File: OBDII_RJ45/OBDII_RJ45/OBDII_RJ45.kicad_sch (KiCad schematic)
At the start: 2 parts, among them J1 Cantact, J2 Conn_01x02

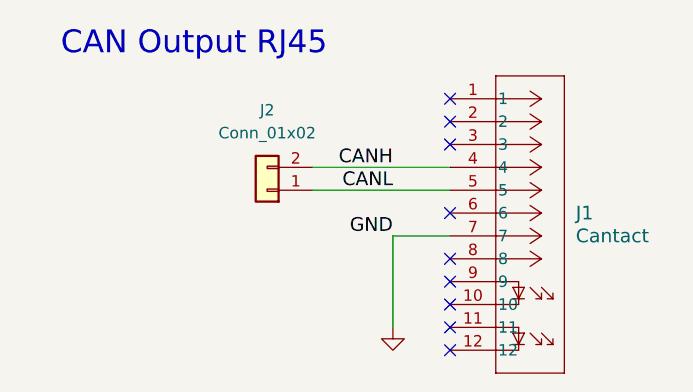
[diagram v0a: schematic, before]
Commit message: feat: add GND between OBDII connector & OBDII_RJ45
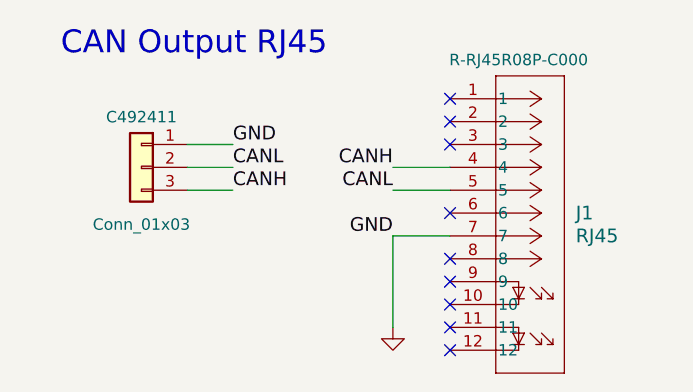
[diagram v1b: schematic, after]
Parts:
- removed J2: Conn_01x02, Connector_PinHeader_2.54mm:PinHeader_1x02_P2.54mm_Vertical, symbol Connector_Generic:Conn_01x02
- added J3: Conn_01x03, Connector_PinHeader_2.54mm:PinHeader_1x03_P2.54mm_Vertical, symbol Connector_Generic:Conn_01x03
- J1: value Cantact -> RJ45; #MANUF (none) -> R-RJ45R08P-C000
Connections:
- net CANH: now also J3.3 (Pin_3)
- net CANL: now also J3.2 (Pin_2)
- net GND: now also J3.1 (Pin_1)
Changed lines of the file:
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@@
 	(wire
 		(pts
-			(xy 43.18 31.75) (xy 58.42 31.75)
-		)
-		(stroke
-			(width 0)
-			(type default)
-		)
-	)
-	(wire
-		(pts
-			(xy 43.18 34.29) (xy 58.42 34.29)
+			(xy 52.07 34.29) (xy 58.42 34.29)
+		)
+		(stroke
+			(width 0)
+			(type default)
+		)
+	)
+	(wire
+		(pts
+			(xy 29.21 34.29) (xy 34.29 34.29)
+		)
+		(stroke
+			(width 0)
+			(type default)
+		)
+	)
+	(wire
+		(pts
+			(xy 52.07 31.75) (xy 58.42 31.75)
+		)
+		(stroke
+			(width 0)
+			(type default)
+		)
+	)
+	(wire
+		(pts
+			(xy 29.21 29.21) (xy 34.29 29.21)
+		)
+		(stroke
+			(width 0)
+			(type default)
+		)
+	)
+	(wire
+		(pts
+			(xy 29.21 31.75) (xy 34.29 31.75)
 		)
 		(stroke
@@
 		)
 	)
+	(label "GND"
+		(at 34.29 29.21 0)
+		(effects
+			(font
+				(size 1.524 1.524)
+			)
+			(justify left bottom)
+		)
+	)
 	(label "CANH"
 		(at 52.07 31.75 180)
@@
 			)
 			(justify right bottom)
+		)
+	)
+	(label "CANL"
+		(at 34.29 31.75 0)
+		(effects
+			(font
+				(size 1.524 1.524)
+			)
+			(justify left bottom)
+		)
+	)
+	(label "CANH"
+		(at 34.29 34.29 0)
+		(effects
+			(font
+				(size 1.524 1.524)
+			)
+			(justify left bottom)
 		)
 	)
@@
 			)
 		)
-		(property "Value" "Cantact"
+		(property "Value" "RJ45"
 			(at 72.39 39.3699 0)
 			(effects
@@
 			)
 		)
-		(property "Datasheet" "R-RJ45R08P-C000"
+		(property "Datasheet" "https://www.lcsc.com/datasheet/lcsc_datasheet_2411121108_Ckmtw-Shenzhen-Cankemeng-R-RJ45R08P-C000_C386757.pdf"
 			(at 56.896 18.796 0)
 			(effects
@@
 				)
 				(hide yes)
+			)
+		)
+		(property "#MANUF" "R-RJ45R08P-C000"
+			(at 66.04 19.812 0)
+			(effects
+				(font
+					(size 1.27 1.27)
+				)
 			)
 		)
@@
 	)
 	(symbol
-		(lib_id "Connector_Generic:Conn_01x02")
-		(at 38.1 34.29 180)
+		(lib_id "Connector_Generic:Conn_01x03")
+		(at 24.13 31.75 0)
+		(mirror y)
 		(unit 1)
 		(exclude_from_sim no)
@@
 		(on_board yes)
 		(dnp no)
-		(fields_autoplaced yes)
-		(property "Reference" "J2"
-			(at 38.1 25.4 0)
-			(effects
-				(font
-					(size 1.27 1.27)
-				)
-			)
-		)
-		(property "Value" "Conn_01x02"
-			(at 38.1 27.94 0)
-			(effects
-				(font
-					(size 1.27 1.27)
-				)
-			)
-		)
-		(property "Footprint" "Connector_PinHeader_2.54mm:PinHeader_1x02_P2.54mm_Vertical"
-			(at 38.1 34.29 0)
-			(effects
-				(font
-					(size 1.27 1.27)
-				)
-				(hide yes)
-			)
-		)
-		(property "Datasheet" "~"
-			(at 38.1 34.29 0)
-			(effects
-				(font
-					(size 1.27 1.27)
-				)
-				(hide yes)
-			)
-		)
-		(property "Description" "Generic connector, single row, 01x02, script generated (kicad-library-utils/schlib/autogen/connector/)"
-			(at 38.1 34.29 0)
-			(effects
-				(font
-					(size 1.27 1.27)
-				)
-				(hide yes)
-			)
-		)
-		(property "#MANUF" ""
-			(at 38.1 34.29 0)
+		(property "Reference" "J3"
+			(at 24.13 40.64 0)
+			(effects
+				(font
+					(size 1.27 1.27)
+				)
+				(hide yes)
+			)
+		)
+		(property "Value" "Conn_01x03"
+			(at 24.13 38.1 0)
+			(effects
+				(font
+					(size 1.27 1.27)
+				)
+			)
+		)
+		(property "Footprint" "Connector_PinHeader_2.54mm:PinHeader_1x03_P2.54mm_Vertical"
+			(at 24.13 31.75 0)
+			(effects
+				(font
+					(size 1.27 1.27)
+				)
+				(hide yes)
+			)
+		)
+		(property "Datasheet" "https://www.lcsc.com/datasheet/lcsc_datasheet_2409302300_XFCN-PZ254R-11-03P_C492411.pdf"
+			(at 24.13 31.75 0)
+			(effects
+				(font
+					(size 1.27 1.27)
+				)
+				(hide yes)
+			)
+		)
+		(property "Description" "Generic connector, single row, 01x03, script generated (kicad-library-utils/schlib/autogen/connector/)"
+			(at 24.13 31.75 0)
+			(effects
+				(font
+					(size 1.27 1.27)
+				)
+				(hide yes)
+			)
+		)
+		(property "#MANUF" "PZ254R-11-03P"
+			(at 24.13 31.75 0)
 			(effects
 				(font
@@
 		)
 		(property "PROVEEDOR" ""
-			(at 38.1 34.29 0)
-			(effects
-				(font
-					(size 1.27 1.27)
-				)
-				(hide yes)
+			(at 24.13 31.75 0)
+			(effects
+				(font
+					(size 1.27 1.27)
+				)
+				(hide yes)
+			)
+		)
+		(property "LCSC#" "C492411"
+			(at 24.13 26.162 0)
+			(effects
+				(font
+					(size 1.27 1.27)
+				)
 			)
 		)
@@
 		)
 		(pin "1"
+		)
+		(pin "3"
 		)
 		(instances
 			(project "OBDII_RJ45"
 				(path "/2550f002-d348-4526-bc52-f9a1d613dc79"
-					(reference "J2")
+					(reference "J3")
 					(unit 1)
 				)

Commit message: feat(Hw):Update_Labels
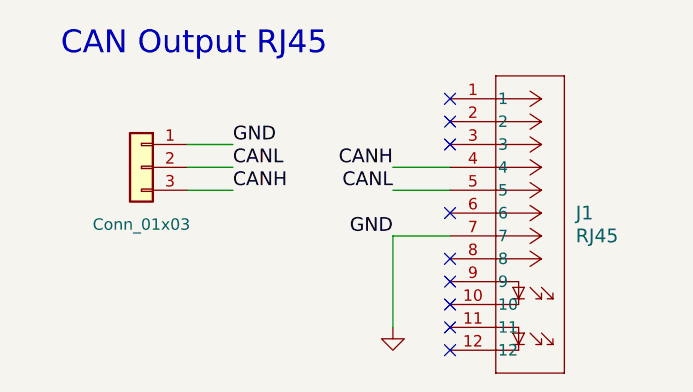
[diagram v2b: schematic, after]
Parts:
- J1: #MANUF R-RJ45R08P-C000 -> (none); manf# R-RJ45R08P-C000 -> (none)
- J3: #MANUF PZ254R-11-03P -> (none)
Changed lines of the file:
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@@
 			)
 		)
-		(property "manf#" "R-RJ45R08P-C000"
+		(property "manf#" ""
 			(at 68.834 20.32 0)
 			(effects
@@
 			)
 		)
-		(property "#MANUF" "R-RJ45R08P-C000"
+		(property "#MANUF" ""
 			(at 66.04 19.812 0)
 			(effects
@@
 			)
 		)
-		(property "#MANUF" "PZ254R-11-03P"
+		(property "#MANUF" ""
 			(at 24.13 31.75 0)
 			(effects
@@
 					(size 1.27 1.27)
 				)
+				(hide yes)
 			)
 		)

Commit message: Fix: CANbus routing for OBDII_RJ45
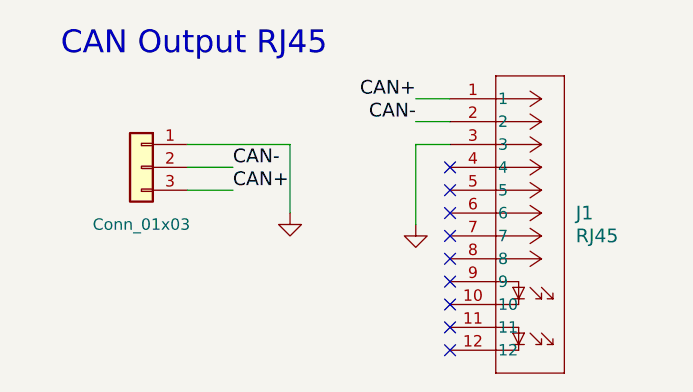
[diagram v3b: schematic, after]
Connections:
- net GND: now also J1.3; no longer J1.7
- net CAN+: now reaches J1.1
- net CAN+: now also J3.3 (Pin_3)
- net CAN-: now reaches J1.2
- net CAN-: now also J3.2 (Pin_2)
- net CANH: no longer names the net of J1.4
- net CANH: no longer J3.3 (Pin_3)
- net CANL: no longer names the net of J1.5
- net CANL: no longer J3.2 (Pin_2)
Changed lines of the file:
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@@
+	)
+	(no_connect
+		(at 58.42 31.75)
+	)
+	(no_connect
+		(at 58.42 34.29)
+	)
+	(no_connect
+		(at 58.42 39.37)
 	)
 	(no_connect
@@
 	)
 	(no_connect
-		(at 58.42 24.13)
-	)
-	(no_connect
 		(at 58.42 49.53)
 	)
@@
 	)
 	(no_connect
-		(at 58.42 26.67)
-	)
-	(no_connect
 		(at 58.42 52.07)
 	)
 	(no_connect
-		(at 58.42 29.21)
-	)
-	(no_connect
 		(at 58.42 44.45)
 	)
 	(wire
 		(pts
-			(xy 52.07 39.37) (xy 58.42 39.37)
-		)
-		(stroke
-			(width 0)
-			(type default)
-		)
-	)
-	(wire
-		(pts
-			(xy 52.07 39.37) (xy 52.07 49.53)
-		)
-		(stroke
-			(width 0)
-			(type default)
-		)
-	)
-	(wire
-		(pts
-			(xy 52.07 34.29) (xy 58.42 34.29)
+			(xy 54.61 38.1) (xy 54.61 29.21)
+		)
+		(stroke
+			(width 0)
+			(type default)
+		)
+	)
+	(wire
+		(pts
+			(xy 40.64 29.21) (xy 40.64 36.83)
+		)
+		(stroke
+			(width 0)
+			(type default)
+		)
+	)
+	(wire
+		(pts
+			(xy 54.61 24.13) (xy 58.42 24.13)
+		)
+		(stroke
+			(width 0)
+			(type default)
+		)
+	)
+	(wire
+		(pts
+			(xy 54.61 26.67) (xy 58.42 26.67)
 		)
 		(stroke
@@
 	(wire
 		(pts
-			(xy 52.07 31.75) (xy 58.42 31.75)
-		)
-		(stroke
-			(width 0)
-			(type default)
-		)
-	)
-	(wire
-		(pts
-			(xy 29.21 29.21) (xy 34.29 29.21)
+			(xy 54.61 29.21) (xy 58.42 29.21)
+		)
+		(stroke
+			(width 0)
+			(type default)
+		)
+	)
+	(wire
+		(pts
+			(xy 29.21 29.21) (xy 40.64 29.21)
 		)
 		(stroke
@@
 		)
 	)
-	(label "CANL"
-		(at 52.07 34.29 180)
+	(label "CAN+"
+		(at 34.29 34.29 0)
 		(effects
 			(font
 				(size 1.524 1.524)
 			)
-			(justify right bottom)
-		)
-	)
-	(label "GND"
-		(at 34.29 29.21 0)
+			(justify left bottom)
+		)
+	)
+	(label "CAN-"
+		(at 54.61 26.67 180)
 		(effects
 			(font
 				(size 1.524 1.524)
 			)
-			(justify left bottom)
-		)
-	)
-	(label "CANH"
-		(at 52.07 31.75 180)
-		(effects
-			(font
-				(size 1.524 1.524)
-			)
 			(justify right bottom)
 		)
 	)
-	(label "GND"
-		(at 52.07 39.37 180)
-		(effects
-			(font
-				(size 1.524 1.524)
-			)
-			(justify right bottom)
-		)
-	)
-	(label "CANL"
+	(label "CAN-"
 		(at 34.29 31.75 0)
 		(effects
@@
 		)
 	)
-	(label "CANH"
-		(at 34.29 34.29 0)
+	(label "CAN+"
+		(at 54.61 24.13 180)
 		(effects
 			(font
 				(size 1.524 1.524)
 			)
-			(justify left bottom)
+			(justify right bottom)
 		)
 	)
@@
 		(lib_name "GND_27")
 		(lib_id "cantact-rescue:GND")
-		(at 52.07 49.53 0)
+		(at 54.61 38.1 0)
 		(unit 1)
 		(exclude_from_sim no)
@@
 		(dnp no)
 		(property "Reference" "#PWR023"
-			(at 52.07 49.53 0)
+			(at 54.61 38.1 0)
 			(effects
 				(font
@@
 		)
 		(property "Value" "GND"
-			(at 52.07 51.308 0)
+			(at 54.61 39.878 0)
 			(effects
 				(font
@@
 		)
 		(property "Footprint" ""
-			(at 52.07 49.53 0)
+			(at 54.61 38.1 0)
 			(effects
 				(font
@@
 		)
 		(property "Datasheet" ""
-			(at 52.07 49.53 0)
+			(at 54.61 38.1 0)
 			(effects
 				(font
@@
 		)
 		(property "Description" ""
-			(at 52.07 49.53 0)
+			(at 54.61 38.1 0)
 			(effects
 				(font
@@
 					(unit 1)
 				)
+			)
+		)
+	)
+	(symbol
+		(lib_name "GND_27")
+		(lib_id "cantact-rescue:GND")
+		(at 40.64 36.83 0)
+		(unit 1)
+		(exclude_from_sim no)
+		(in_bom yes)
+		(on_board yes)
+		(dnp no)
+		(property "Reference" "#PWR024"
+			(at 40.64 36.83 0)
+			(effects
+				(font
+					(size 0.762 0.762)
+				)
+				(hide yes)
+			)
+		)
+		(property "Value" "GND"
+			(at 40.64 38.608 0)
+			(effects
+				(font
+					(size 0.762 0.762)
+				)
+				(hide yes)
+			)
+		)
+		(property "Footprint" ""
+			(at 40.64 36.83 0)
+			(effects
+				(font
+					(size 1.524 1.524)
+				)
+			)
+		)
+		(property "Datasheet" ""
+			(at 40.64 36.83 0)
+			(effects
+				(font
+					(size 1.524 1.524)
+				)
+			)
+		)
+		(property "Description" ""
+			(at 40.64 36.83 0)
+			(effects
+				(font
+					(size 1.27 1.27)
+				)
+			)
+		)
+		(pin "1"
+		)
+		(instances
+			(project "OBDII_RJ45"
+				(path "/2550f002-d348-4526-bc52-f9a1d613dc79"
+					(reference "#PWR024")
+					(unit 1)
+				)
